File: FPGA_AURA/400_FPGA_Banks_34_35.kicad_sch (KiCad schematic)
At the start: 1 part, among them U1 XC7A35T-2FTG256C

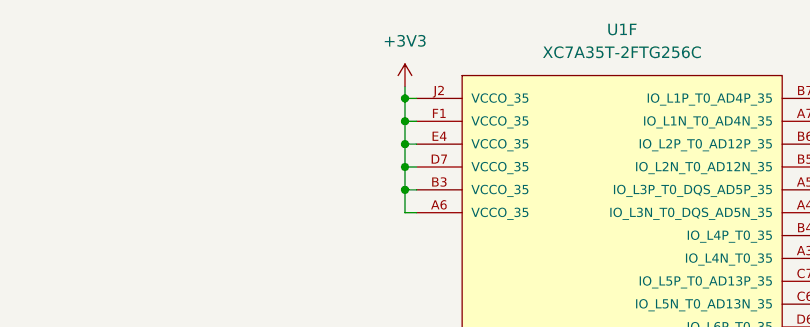
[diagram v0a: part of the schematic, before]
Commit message: Added USB power schottky and started DDR3L
Transferring from laptop to PC to decide DDR3 pins.
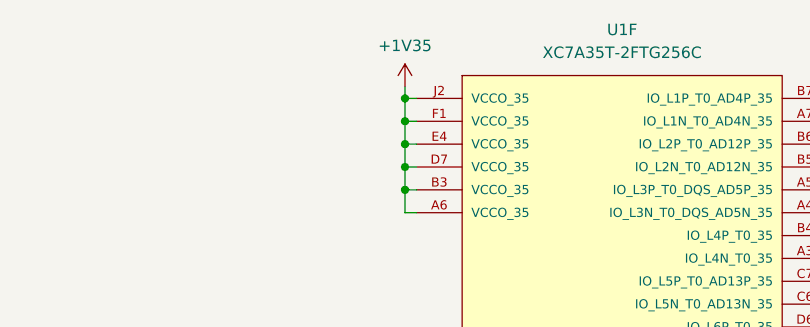
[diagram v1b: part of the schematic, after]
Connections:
- net +3V3: no longer U1.A6 (VCCO_35), U1.B3 (VCCO_35), U1.D7 (VCCO_35), U1.E4 (VCCO_35), U1.F1 (VCCO_35), U1.J2 (VCCO_35)
- new net +1V35: U1.A6 (VCCO_35), U1.B3 (VCCO_35), U1.D7 (VCCO_35), U1.E4 (VCCO_35), U1.F1 (VCCO_35), U1.J2 (VCCO_35)
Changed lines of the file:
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@@
 		(on_board yes)
 		(dnp no)
-		(fields_autoplaced yes)
 		(property "Reference" "#PWR021"
 			(at 176.53 34.29 0)
@@
 			)
 		)
-		(property "Value" "+3V3"
-			(at 176.53 25.4 0)
+		(property "Value" "+1V35"
+			(at 176.53 25.908 0)
 			(effects
 				(font

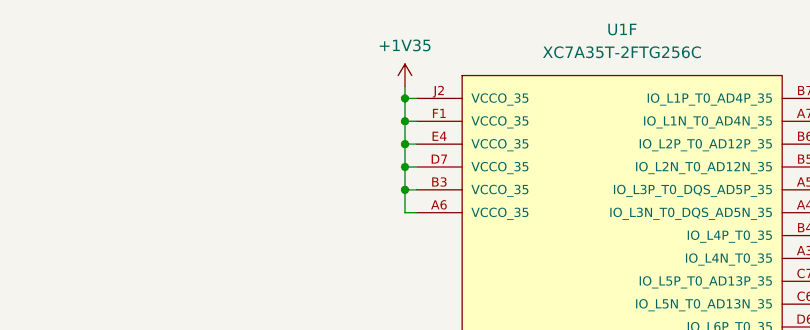
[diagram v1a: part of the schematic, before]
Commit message: Moving to PC.
Placed the VTT termination resistors roughly, rotated the DDR IC 180, and deleted the initial draft of routing.
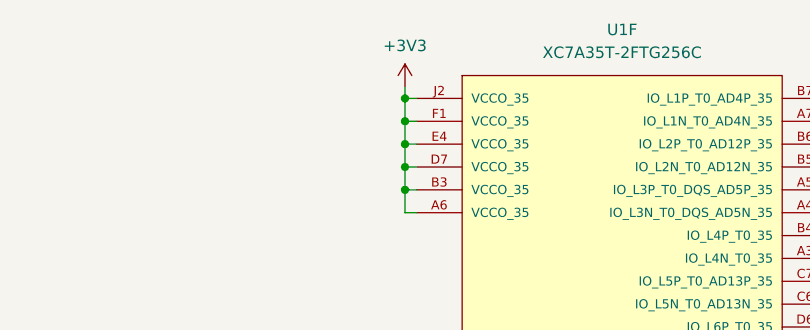
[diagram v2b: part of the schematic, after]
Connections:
- net +1V35 is gone; now on net +3V3: U1.A6 (VCCO_35), U1.B3 (VCCO_35), U1.D7 (VCCO_35), U1.E4 (VCCO_35), U1.F1 (VCCO_35), U1.J2 (VCCO_35)
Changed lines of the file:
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@@
 			)
 		)
-		(property "Value" "+1V35"
+		(property "Value" "+3V3"
 			(at 176.53 25.908 0)
 			(effects
